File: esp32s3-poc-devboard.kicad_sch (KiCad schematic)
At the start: 0 parts

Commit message: AMS117 3.3v ldo
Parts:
- added C17, C19: 10u, symbol Device:C
- added C18, C20: 0.1u, symbol Device:C
- added D2: LED, symbol Device:LED
- added R14: 5k1, symbol Device:R
- added U1: ESP32-S3, Package_DFN_QFN:QFN-56-1EP_7x7mm_P0.4mm_EP5.6x5.6mm, symbol PCM_Espressif:ESP32-S3
- added U4: AMS1117-3.3, Package_TO_SOT_SMD:SOT-223-3_TabPin2, symbol Regulator_Linear:AMS1117-3.3
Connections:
- new net: D2.2 (A), R14.2
- new net: U1.55 (VDDA), U1.56 (VDDA)
- new net +3V3: C19.1, C20.1, R14.1, U4.2 (VO)
- new net +5V: C17.1, C18.1, U4.3 (VI)
- new net GND: C17.2, C18.2, C19.2, C20.2, D2.1 (K), U4.1 (GND)
- new net VDD3P3: U1.2 (VDD3P3), U1.3 (VDD3P3)
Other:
- note added: "AMS117 3.3v"

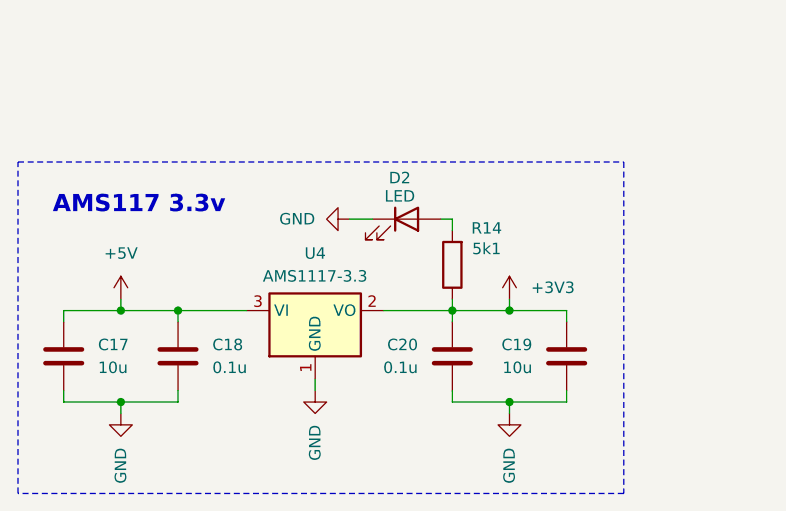
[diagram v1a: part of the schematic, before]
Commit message: updated AMS117 3.3v ldo
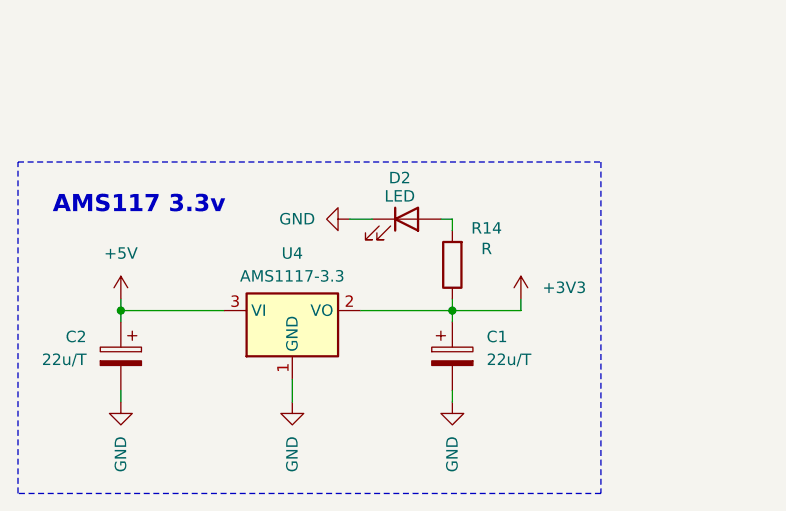
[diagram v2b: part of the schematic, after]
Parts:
- removed C17, C19: 10u, symbol Device:C
- removed C18, C20: 0.1u, symbol Device:C
- added C1, C2: 22u/T, symbol Device:C_Polarized
- R14: value 5k1 -> R
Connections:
- net +3V3: now also C1.1
- net +5V: now also C2.1
- net GND: now also C1.2, C2.2
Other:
- moved on the sheet: U4

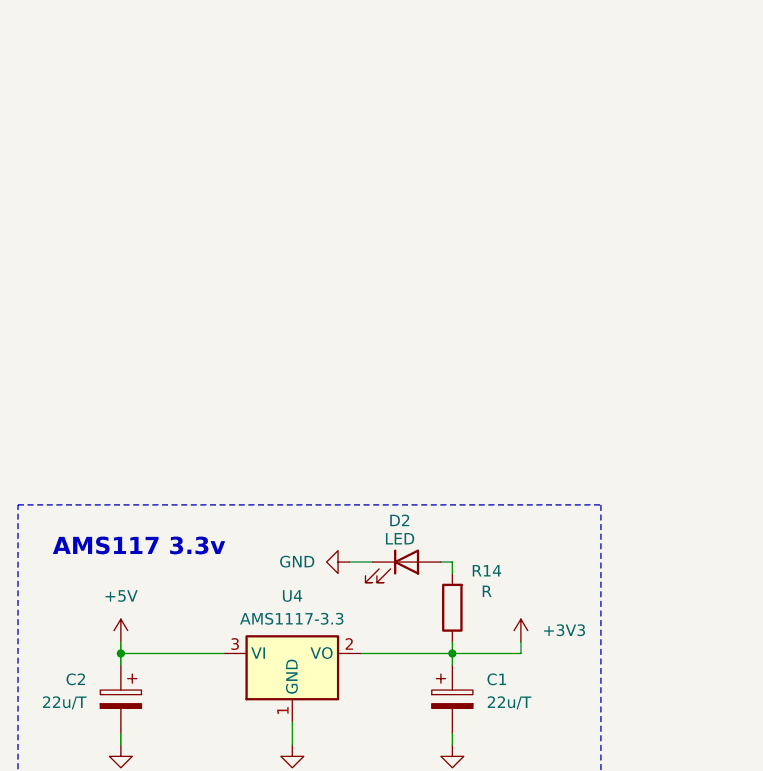
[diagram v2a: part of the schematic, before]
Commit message: add XC6206 3.3v ldo
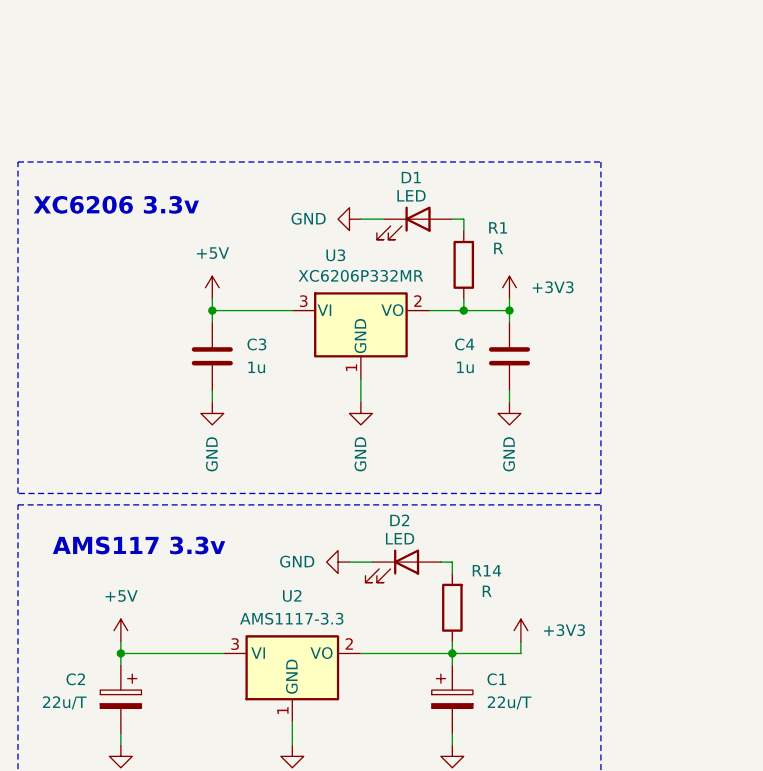
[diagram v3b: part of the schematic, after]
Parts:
- added C3, C4: 1u, symbol Device:C
- added D1: LED, symbol Device:LED
- added R1: R, symbol Device:R
- added U3: XC6206P332MR, Package_TO_SOT_SMD:SOT-23-3, symbol Regulator_Linear:XC6206PxxxMR
- renumbered U4 to U2
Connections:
- net +3V3: now also C4.1, R1.1, U3.2 (VO)
- net +5V: now also C3.1, U3.3 (VI)
- net GND: now also C3.2, C4.2, D1.1 (K), U3.1 (GND)
- new net: D1.2 (A), R1.2
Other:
- note added: "XC6206 3.3v"

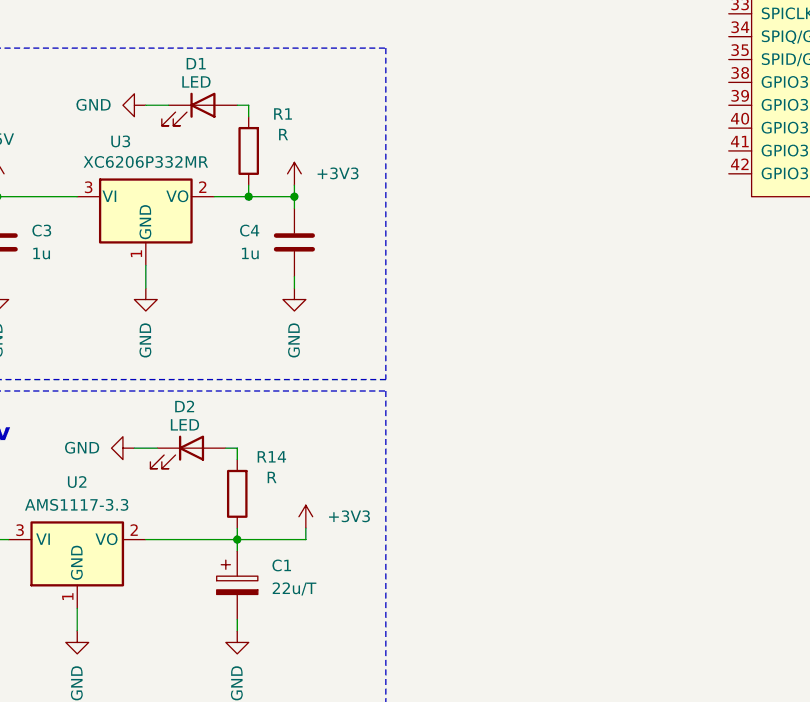
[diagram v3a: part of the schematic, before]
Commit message: add ldo selection jumper
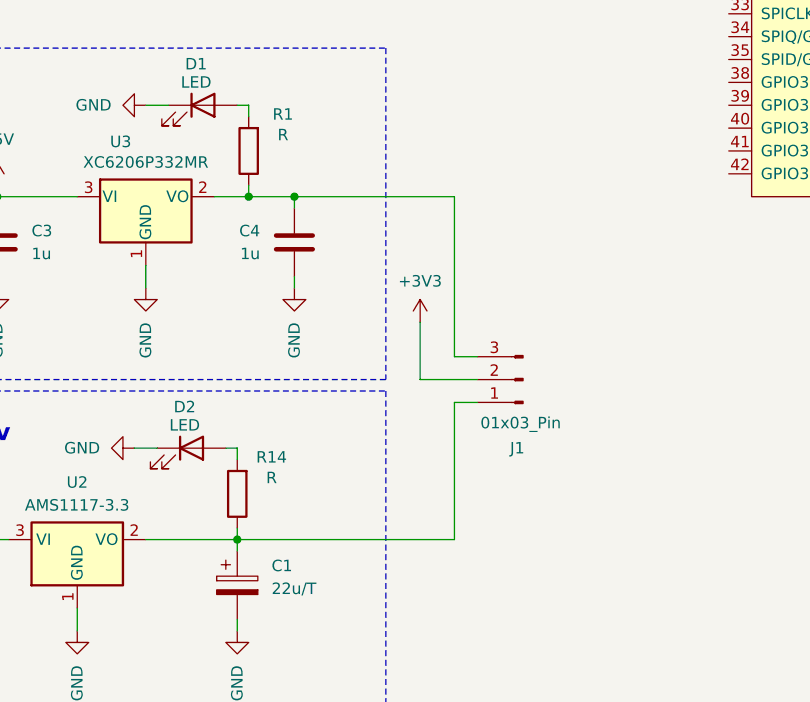
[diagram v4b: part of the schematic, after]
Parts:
- added J1: 01x03_Pin, symbol Connector:Conn_01x03_Pin
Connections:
- net +3V3: now also J1.2 (Pin_2); no longer C1.1, C4.1, R1.1, R14.1, U2.2 (VO), U3.2 (VO)
- new net: C4.1, J1.3 (Pin_3), R1.1, U3.2 (VO)
- new net: C1.1, J1.1 (Pin_1), R14.1, U2.2 (VO)
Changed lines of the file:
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@@
-	(wire
-		(pts
-			(xy 72.39 134.62) (xy 72.39 135.89)
-		)
-		(stroke
-			(width 0)
-			(type default)
-		)
-	)
 	(wire
 		(pts
@@
 	(wire
 		(pts
+			(xy 90.17 135.89) (xy 90.17 153.67)
+		)
+		(stroke
+			(width 0)
+			(type default)
+		)
+	)
+	(wire
+		(pts
 			(xy 55.88 143.51) (xy 55.88 146.05)
 		)
@@
 	(wire
 		(pts
+			(xy 90.17 158.75) (xy 90.17 173.99)
+		)
+		(stroke
+			(width 0)
+			(type default)
+		)
+	)
+	(wire
+		(pts
 			(xy 29.21 175.26) (xy 29.21 173.99)
 		)
@@
 	(wire
 		(pts
+			(xy 90.17 173.99) (xy 66.04 173.99)
+		)
+		(stroke
+			(width 0)
+			(type default)
+		)
+	)
+	(wire
+		(pts
 			(xy 66.04 125.73) (xy 67.31 125.73)
 		)
@@
 	(wire
 		(pts
+			(xy 72.39 135.89) (xy 90.17 135.89)
+		)
+		(stroke
+			(width 0)
+			(type default)
+		)
+	)
+	(wire
+		(pts
 			(xy 55.88 125.73) (xy 58.42 125.73)
 		)
@@
 	(wire
 		(pts
+			(xy 86.36 149.86) (xy 86.36 156.21)
+		)
+		(stroke
+			(width 0)
+			(type default)
+		)
+	)
+	(wire
+		(pts
 			(xy 67.31 135.89) (xy 63.5 135.89)
 		)
@@
 	(wire
 		(pts
-			(xy 66.04 173.99) (xy 73.66 173.99)
+			(xy 92.71 158.75) (xy 90.17 158.75)
 		)
 		(stroke
@@
 	(wire
 		(pts
+			(xy 86.36 156.21) (xy 92.71 156.21)
+		)
+		(stroke
+			(width 0)
+			(type default)
+		)
+	)
+	(wire
+		(pts
 			(xy 66.04 172.72) (xy 66.04 173.99)
 		)
@@
 	(wire
 		(pts
-			(xy 73.66 173.99) (xy 73.66 172.72)
-		)
-		(stroke
-			(width 0)
-			(type default)
-		)
-	)
-	(wire
-		(pts
 			(xy 67.31 125.73) (xy 67.31 127)
+		)
+		(stroke
+			(width 0)
+			(type default)
+		)
+	)
+	(wire
+		(pts
+			(xy 90.17 153.67) (xy 92.71 153.67)
 		)
 		(stroke
@@
 	)
 	(symbol
-		(lib_id "power:+3V3")
-		(at 72.39 134.62 0)
-		(unit 1)
-		(exclude_from_sim no)
-		(in_bom yes)
-		(on_board yes)
-		(dnp no)
-		(property "Reference" "#PWR06"
-			(at 72.39 138.43 0)
-			(effects
-				(font
-					(size 1.27 1.27)
-				)
-				(hide yes)
-			)
-		)
-		(property "Value" "+3V3"
-			(at 77.216 133.35 0)
-			(effects
-				(font
-					(size 1.27 1.27)
-				)
-			)
-		)
-		(property "Footprint" ""
-			(at 72.39 134.62 0)
-			(effects
-				(font
-					(size 1.27 1.27)
-				)
-				(hide yes)
-			)
-		)
-		(property "Datasheet" ""
-			(at 72.39 134.62 0)
-			(effects
-				(font
-					(size 1.27 1.27)
-				)
-				(hide yes)
-			)
-		)
-		(property "Description" "Power symbol creates a global label with name \"+3V3\""
-			(at 72.39 134.62 0)
-			(effects
-				(font
-					(size 1.27 1.27)
-				)
-				(hide yes)
-			)
-		)
-		(pin "1"
-		)
-		(instances
-			(project "esp32s3-poc-devboard"
-				(path "/a6beb550-83d0-4746-bc61-cde76b7466a3"
-					(reference "#PWR06")
-					(unit 1)
-				)
-			)
-		)
-	)
-	(symbol
 		(lib_id "power:GND")
 		(at 55.88 146.05 0)
@@
 	)
 	(symbol
+		(lib_id "Connector:Conn_01x03_Pin")
+		(at 97.79 156.21 180)
+		(unit 1)
+		(exclude_from_sim no)
+		(in_bom yes)
+		(on_board yes)
+		(dnp no)
+		(property "Reference" "J1"
+			(at 97.155 163.83 0)
+			(effects
+				(font
+					(size 1.27 1.27)
+				)
+			)
+		)
+		(property "Value" "01x03_Pin"
+			(at 97.536 161.036 0)
+			(effects
+				(font
+					(size 1.27 1.27)
+				)
+			)
+		)
+		(property "Footprint" ""
+			(at 97.79 156.21 0)
+			(effects
+				(font
+					(size 1.27 1.27)
+				)
+				(hide yes)
+			)
+		)
+		(property "Datasheet" "~"
+			(at 97.79 156.21 0)
+			(effects
+				(font
+					(size 1.27 1.27)
+				)
+				(hide yes)
+			)
+		)
+		(property "Description" "Generic connector, single row, 01x03, script generated"
+			(at 97.79 156.21 0)
+			(effects
+				(font
+					(size 1.27 1.27)
+				)
+				(hide yes)
+			)
+		)
+		(pin "2"
+		)
+		(pin "3"
+		)
+		(pin "1"
+		)
+		(instances
+			(project ""
+				(path "/a6beb550-83d0-4746-bc61-cde76b7466a3"
+					(reference "J1")
+					(unit 1)
+				)
+			)
+		)
+	)
+	(symbol
 		(lib_id "Regulator_Linear:XC6206PxxxMR")
 		(at 55.88 135.89 0)
@@
 	(symbol
 		(lib_id "power:+3V3")
-		(at 73.66 172.72 0)
+		(at 86.36 149.86 0)
 		(unit 1)
 		(exclude_from_sim no)
@@
 		(dnp no)
 		(property "Reference" "#PWR023"
-			(at 73.66 176.53 0)
+			(at 86.36 153.67 0)
 			(effects
 				(font
@@
 		)
 		(property "Value" "+3V3"
-			(at 78.486 171.45 0)
+			(at 86.36 145.288 0)
 			(effects
 				(font
@@
 		)
 		(property "Footprint" ""
-			(at 73.66 172.72 0)
+			(at 86.36 149.86 0)
 			(effects
 				(font
@@
 		)
 		(property "Datasheet" ""
-			(at 73.66 172.72 0)
+			(at 86.36 149.86 0)
 			(effects
 				(font
@@
 		)
 		(property "Description" "Power symbol creates a global label with name \"+3V3\""
-			(at 73.66 172.72 0)
-			(effects
-				(font
+			(at 86.36 149.86 0)
+			(effects
+				(font

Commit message: add notes txt
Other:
- note added: "Notes: - Pi sur VBUS"
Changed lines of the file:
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@@
+		)
+	)
+	(text "Notes:\n- Pi sur VBUS"
+		(exclude_from_sim no)
+		(at 16.002 16.764 0)
+		(effects
+			(font
+				(size 1.27 1.27)
+			)
+			(justify left)
 		)
 	)

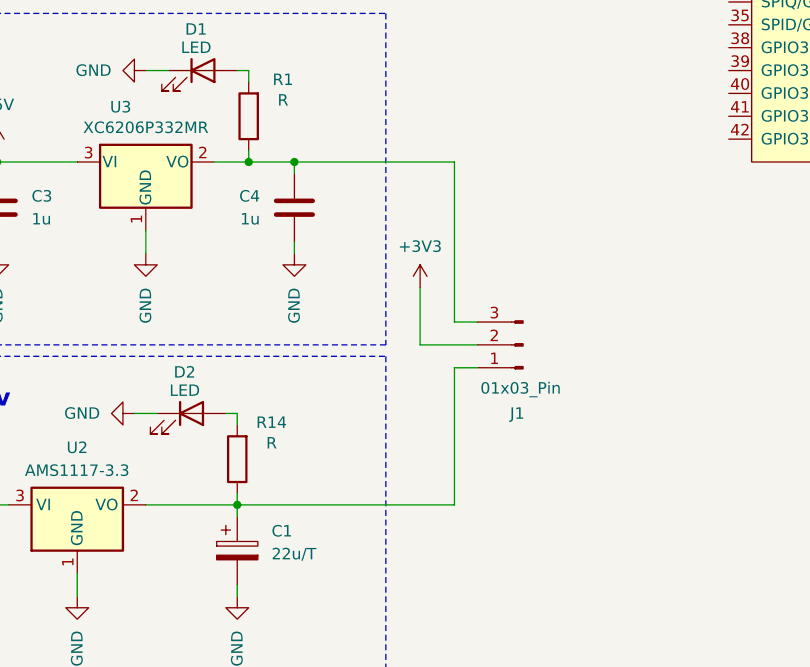
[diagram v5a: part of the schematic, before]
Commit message: changed pwr header to jumper
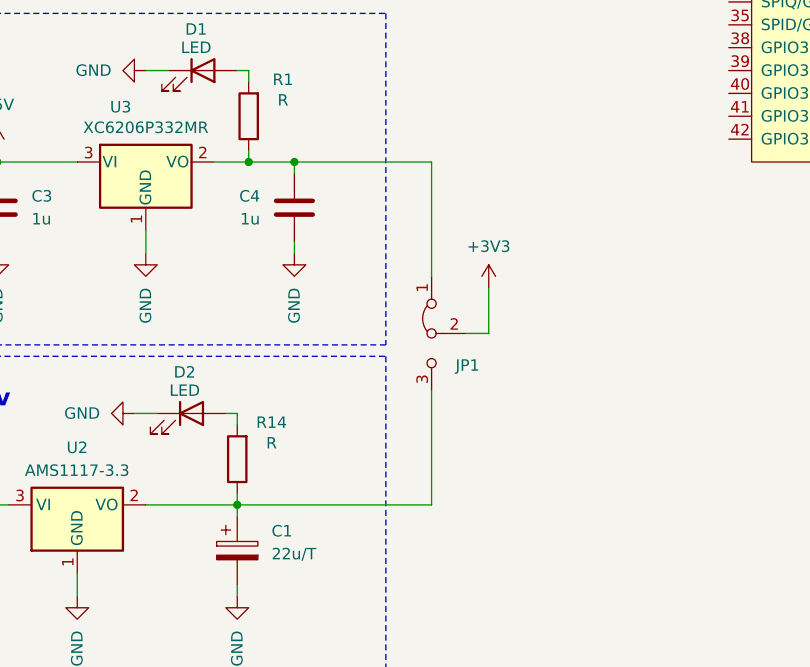
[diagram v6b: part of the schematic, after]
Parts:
- removed J1: 01x03_Pin, symbol Connector:Conn_01x03_Pin
- added JP1: PWR, symbol Jumper:Jumper_3_Bridged12
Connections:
- net +3V3: now also JP1.2 (C)
- net at C4.1, R1.1, U3.2 (VO): now also JP1.1 (A)
- net at C1.1, R14.1, U2.2 (VO): now also JP1.3 (B)
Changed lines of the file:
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@@
+	(wire
+		(pts
+			(xy 91.44 154.94) (xy 93.98 154.94)
+		)
+		(stroke
+			(width 0)
+			(type default)
+		)
+	)
+	(wire
+		(pts
+			(xy 93.98 154.94) (xy 93.98 149.86)
+		)
+		(stroke
+			(width 0)
+			(type default)
+		)
+	)
 	(wire
 		(pts
@@
 	(wire
 		(pts
-			(xy 90.17 135.89) (xy 90.17 153.67)
-		)
-		(stroke
-			(width 0)
-			(type default)
-		)
-	)
-	(wire
-		(pts
 			(xy 55.88 143.51) (xy 55.88 146.05)
 		)
@@
 	(wire
 		(pts
-			(xy 90.17 158.75) (xy 90.17 173.99)
+			(xy 87.63 148.59) (xy 87.63 135.89)
 		)
 		(stroke
@@
 	(wire
 		(pts
-			(xy 90.17 173.99) (xy 66.04 173.99)
+			(xy 66.04 173.99) (xy 87.63 173.99)
 		)
 		(stroke
@@
 	(wire
 		(pts
-			(xy 72.39 135.89) (xy 90.17 135.89)
+			(xy 72.39 135.89) (xy 87.63 135.89)
 		)
 		(stroke
@@
 	(wire
 		(pts
+			(xy 87.63 173.99) (xy 87.63 161.29)
+		)
+		(stroke
+			(width 0)
+			(type default)
+		)
+	)
+	(wire
+		(pts
 			(xy 39.37 134.62) (xy 39.37 135.89)
 		)
@@
 	(wire
 		(pts
-			(xy 86.36 149.86) (xy 86.36 156.21)
-		)
-		(stroke
-			(width 0)
-			(type default)
-		)
-	)
-	(wire
-		(pts
 			(xy 67.31 135.89) (xy 63.5 135.89)
 		)
@@
 	(wire
 		(pts
-			(xy 92.71 158.75) (xy 90.17 158.75)
-		)
-		(stroke
-			(width 0)
-			(type default)
-		)
-	)
-	(wire
-		(pts
 			(xy 29.21 172.72) (xy 29.21 173.99)
 		)
@@
 	(wire
 		(pts
-			(xy 86.36 156.21) (xy 92.71 156.21)
-		)
-		(stroke
-			(width 0)
-			(type default)
-		)
-	)
-	(wire
-		(pts
 			(xy 66.04 172.72) (xy 66.04 173.99)
 		)
@@
 		(pts
 			(xy 67.31 125.73) (xy 67.31 127)
-		)
-		(stroke
-			(width 0)
-			(type default)
-		)
-	)
-	(wire
-		(pts
-			(xy 90.17 153.67) (xy 92.71 153.67)
 		)
 		(stroke
@@
 	)
 	(symbol
+		(lib_id "Jumper:Jumper_3_Bridged12")
+		(at 87.63 154.94 90)
+		(mirror x)
+		(unit 1)
+		(exclude_from_sim no)
+		(in_bom no)
+		(on_board yes)
+		(dnp no)
+		(property "Reference" "JP1"
+			(at 92.964 158.496 90)
+			(effects
+				(font
+					(size 1.27 1.27)
+				)
+				(justify left)
+			)
+		)
+		(property "Value" "PWR"
+			(at 92.456 159.766 90)
+			(effects
+				(font
+					(size 1.27 1.27)
+				)
+				(justify left)
+				(hide yes)
+			)
+		)
+		(property "Footprint" ""
+			(at 87.63 154.94 0)
+			(effects
+				(font
+					(size 1.27 1.27)
+				)
+				(hide yes)
+			)
+		)
+		(property "Datasheet" "~"
+			(at 87.63 154.94 0)
+			(effects
+				(font
+					(size 1.27 1.27)
+				)
+				(hide yes)
+			)
+		)
+		(property "Description" "Jumper, 3-pole, pins 1+2 closed/bridged"
+			(at 87.63 154.94 0)
+			(effects
+				(font
+					(size 1.27 1.27)
+				)
+				(hide yes)
+			)
+		)
+		(pin "3"
+		)
+		(pin "2"
+		)
+		(pin "1"
+		)
+		(instances
+			(project ""
+				(path "/a6beb550-83d0-4746-bc61-cde76b7466a3"
+					(reference "JP1")
+					(unit 1)
+				)
+			)
+		)
+	)
+	(symbol
 		(lib_id "Device:R")
 		(at 66.04 168.91 180)
@@
 	)
 	(symbol
-		(lib_id "Connector:Conn_01x03_Pin")
-		(at 97.79 156.21 180)
-		(unit 1)
-		(exclude_from_sim no)
-		(in_bom yes)
-		(on_board yes)
-		(dnp no)
-		(property "Reference" "J1"
-			(at 97.155 163.83 0)
-			(effects
-				(font
-					(size 1.27 1.27)
-				)
-			)
-		)
-		(property "Value" "01x03_Pin"
-			(at 97.536 161.036 0)
-			(effects
-				(font
-					(size 1.27 1.27)
-				)
-			)
-		)
-		(property "Footprint" ""
-			(at 97.79 156.21 0)
-			(effects
-				(font
-					(size 1.27 1.27)
-				)
-				(hide yes)
-			)
-		)
-		(property "Datasheet" "~"
-			(at 97.79 156.21 0)
-			(effects
-				(font
-					(size 1.27 1.27)
-				)
-				(hide yes)
-			)
-		)
-		(property "Description" "Generic connector, single row, 01x03, script generated"
-			(at 97.79 156.21 0)
-			(effects
-				(font
-					(size 1.27 1.27)
-				)
-				(hide yes)
-			)
-		)
-		(pin "2"
-		)
-		(pin "3"
-		)
-		(pin "1"
-		)
-		(instances
-			(project ""
-				(path "/a6beb550-83d0-4746-bc61-cde76b7466a3"
-					(reference "J1")
-					(unit 1)
-				)
-			)
-		)
-	)
-	(symbol
 		(lib_id "Regulator_Linear:XC6206PxxxMR")
 		(at 55.88 135.89 0)
@@
 	(symbol
 		(lib_id "power:+3V3")
-		(at 86.36 149.86 0)
+		(at 93.98 149.86 0)
+		(mirror y)
 		(unit 1)
 		(exclude_from_sim no)
@@
 		(dnp no)
 		(property "Reference" "#PWR023"
-			(at 86.36 153.67 0)
+			(at 93.98 153.67 0)
 			(effects
 				(font
@@
 		)
 		(property "Value" "+3V3"
-			(at 86.36 145.288 0)
-			(effects
-				(font
-					(size 1.27 1.27)
-				)
-			)
-		)
-		(property "Footprint" ""
-			(at 86.36 149.86 0)
+			(at 93.98 145.288 0)
+			(effects
+				(font
+					(size 1.27 1.27)
+				)
+			)
+		)
+		(property "Footprint" ""
+			(at 93.98 149.86 0)
 			(effects
 				(font
@@
 		)
 		(property "Datasheet" ""
-			(at 86.36 149.86 0)
+			(at 93.98 149.86 0)
 			(effects
 				(font
@@
 		)
 		(property "Description" "Power symbol creates a global label with name \"+3V3\""
-			(at 86.36 149.86 0)
-			(effects
-				(font
+			(at 93.98 149.86 0)
+			(effects
+				(font

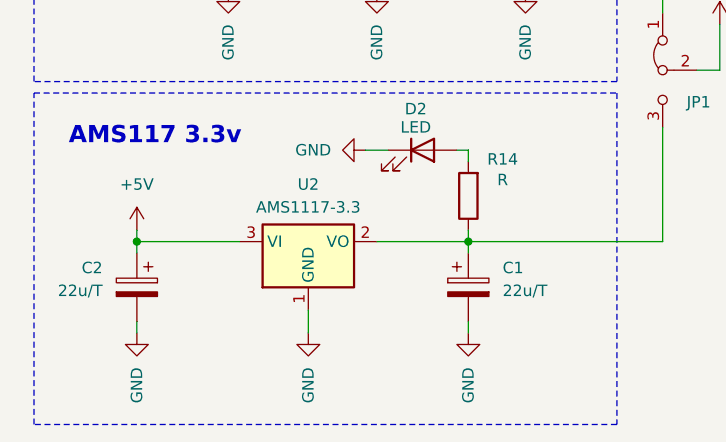
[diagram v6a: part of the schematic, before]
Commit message: change to non-polarized capacitors
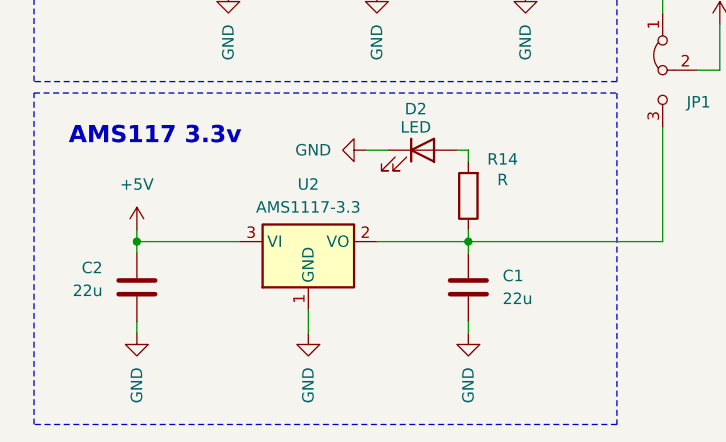
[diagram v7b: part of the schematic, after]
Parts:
- C1, C2: value 22u/T -> 22u; symbol Device:C_Polarized -> Device:C
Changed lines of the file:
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@@
 	)
 	(symbol
-		(lib_id "Device:C_Polarized")
+		(lib_id "Device:C")
 		(at 29.21 179.07 0)
 		(mirror y)
@@
 			)
 		)
-		(property "Value" "22u/T"
+		(property "Value" "22u"
 			(at 25.4 179.4509 0)
 			(effects
@@
 			)
 		)
-		(property "Description" "Polarized capacitor"
+		(property "Description" "Unpolarized capacitor"
 			(at 29.21 179.07 0)
 			(effects
@@
 	)
 	(symbol
-		(lib_id "Device:C_Polarized")
+		(lib_id "Device:C")
 		(at 66.04 179.07 0)
 		(unit 1)
@@
 		(fields_autoplaced yes)
 		(property "Reference" "C1"
-			(at 69.85 176.9109 0)
+			(at 69.85 177.7999 0)
 			(effects
 				(font
@@
 			)
 		)
-		(property "Value" "22u/T"
-			(at 69.85 179.4509 0)
+		(property "Value" "22u"
+			(at 69.85 180.3399 0)
 			(effects
 				(font
@@
 			)
 		)
-		(property "Description" "Polarized capacitor"
+		(property "Description" "Unpolarized capacitor"
 			(at 66.04 179.07 0)
 			(effects
